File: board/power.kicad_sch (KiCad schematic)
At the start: 29 parts

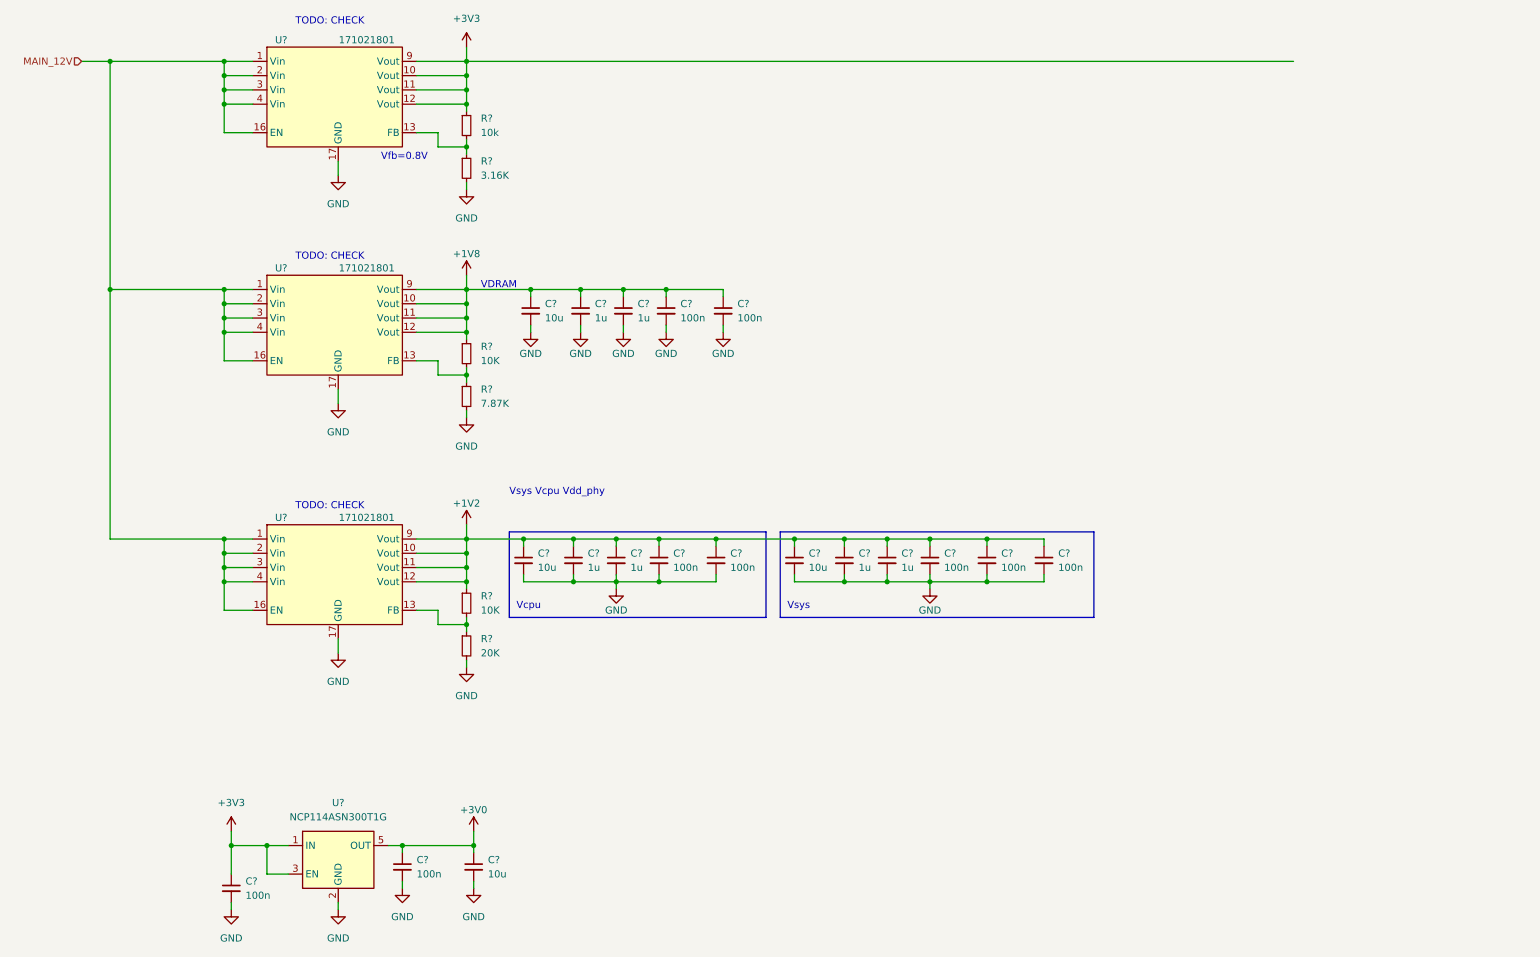
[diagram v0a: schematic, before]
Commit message: schematic update, choose components, creeate footprints
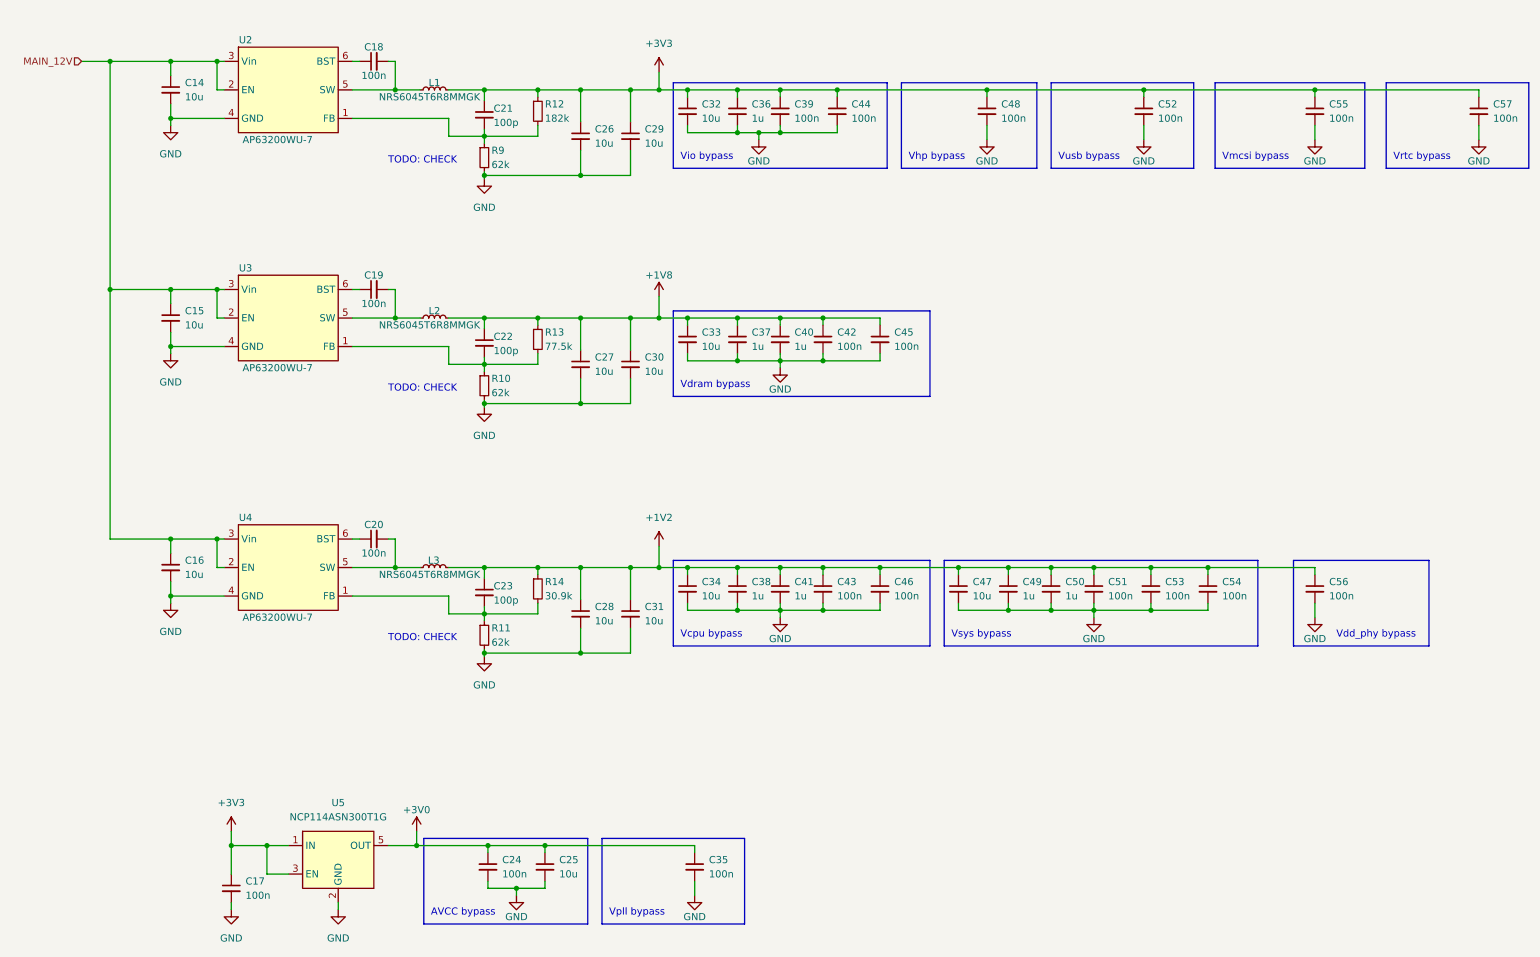
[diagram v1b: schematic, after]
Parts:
- removed R?: 3.16K, symbol Device:R_Small
- removed R? (x2): 10K, symbol Device:R_Small
- removed R?: 20K, symbol Device:R_Small
- removed R?: 7.87K, symbol Device:R_Small
- removed R?: 10k, symbol Device:R_Small
- removed U? (x3): 171021801, symbol v3s:171021801
- added C14, C15, C16, C26, C27, C28, C29, C30, C31, C32: 10u, Capacitor_SMD:C_0603_1608Metric, symbol Device:C_Small
- added C18, C19, C20, C35, C39, C44, C48, C52, C55, C56, C57: 100n, Capacitor_SMD:C_0603_1608Metric, symbol Device:C_Small
- added C21, C22, C23: 100p, Capacitor_SMD:C_0603_1608Metric, symbol Device:C_Small
- added C36: 1u, Capacitor_SMD:C_0603_1608Metric, symbol Device:C_Small
- added L1, L2, L3: NRS6045T6R8MMGK, v3s:NRS6045T6R8, symbol Device:L_Small
- added R10, R11, R9: 62k, Resistor_SMD:R_0603_1608Metric, symbol Device:R_Small
- added R12: 182k, Resistor_SMD:R_0603_1608Metric, symbol Device:R_Small
- added R13: 77.5k, Resistor_SMD:R_0603_1608Metric, symbol Device:R_Small
- added R14: 30.9k, Resistor_SMD:R_0603_1608Metric, symbol Device:R_Small
- added U2, U3, U4: AP63200WU-7, v3s:TSOT26, symbol v3s:AP63200WU-7
- C17, C24, C25, C33, C34, C37, C38, C40, C41, C42, C43, C45, C46, C47, C49, C50, C51, C53, C54: renamed from C?; footprint (none) -> Capacitor_SMD:C_0603_1608Metric
- gave numbers to parts that had none: 1
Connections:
- net +1V2: now also C23.1, C28.1, C31.1, C56.1, L3.2, R14.1
- net +1V8: now also C22.1, C27.1, C30.1, L2.2, R13.1
- net +3V0: now also C35.1
- net +3V3: now also C21.1, C26.1, C29.1, C32.1, C36.1, C39.1, C44.1, C48.1, C52.1, C55.1, C57.1, L1.2, R12.1
- net GND: now also C14.2, C15.2, C16.2, C26.2, C27.2, C28.2, C29.2, C30.2, C31.2, C32.2, C35.2, C36.2, C39.2, C44.2, C48.2, C52.2, C55.2, C56.2, C57.2, R10.2, R11.2, R9.2, U2.4 (GND), U3.4 (GND), U4.4 (GND)
- net MAIN_12V: now also C14.1, C15.1, C16.1, U2.2 (EN), U2.3 (Vin), U3.2 (EN), U3.3 (Vin), U4.2 (EN), U4.3 (Vin)
- new net: C19.1, U3.6 (BST)
- new net: C19.2, L2.1, U3.5 (SW)
- new net: C23.2, R11.1, R14.2, U4.1 (FB)
- new net: C20.2, L3.1, U4.5 (SW)
- new net: C20.1, U4.6 (BST)
- new net: C22.2, R10.1, R13.2, U3.1 (FB)
- new net: C18.2, L1.1, U2.5 (SW)
- new net: C21.2, R12.2, R9.1, U2.1 (FB)
- new net: C18.1, U2.6 (BST)
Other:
- note added: "AVCC bypass"
- note added: "Vcpu bypass"
- note added: "Vdd_phy bypass"
- note added: "Vdram bypass"
- note added: "Vhp bypass"
- note added: "Vio bypass"
- note added: "Vmcsi bypass"
- note added: "Vpll bypass"
- note added: "Vrtc bypass"
- note added: "Vsys bypass"
- note added: "Vusb bypass"
- note removed: "VDRAM"
- note removed: "Vcpu"
- note removed: "Vfb=0.8V"
- note removed: "Vsys"
- note removed: "Vsys Vcpu Vdd_phy"
- moved on the sheet: C24, C25, C33, C34, C37, C38, C40, C41, C42, C43, C45, C46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

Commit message: pcb layout
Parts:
- C25: value 10u -> 1u
- C32, C34, C47: value 10u -> 100n
- C36, C38, C41, C49, C50: value 1u -> 100n
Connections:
- net MAIN_12V renamed +12V
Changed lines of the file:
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@@
+    (stroke (width 0) (type default) (color 0 0 0 0))
+  )
+  (wire (pts (xy 30.48 27.94) (xy 30.48 30.48))
     (stroke (width 0) (type default) (color 0 0 0 0))
   )
@@
       (effects (font (size 1.27 1.27)) (justify left))
     )
-    (property "Value" "10u" (id 1) (at 135.89 40.6462 0)
+    (property "Value" "100n" (id 1) (at 135.89 40.6462 0)
       (effects (font (size 1.27 1.27)) (justify left))
     )
@@
       (effects (font (size 1.27 1.27)) (justify left))
     )
-    (property "Value" "10u" (id 1) (at 110.49 175.2662 0)
+    (property "Value" "1u" (id 1) (at 110.49 175.2662 0)
       (effects (font (size 1.27 1.27)) (justify left))
     )
@@
   )
   (symbol (lib_id "Device:C_Small") (at 205.74 124.46 0) (unit 1)
-    (in_bom yes) (on_board yes) (fields_autoplaced)
-    (property "Reference" "C51" (id 0) (at 208.28 123.1962 0)
-      (effects (font (size 1.27 1.27)) (justify left))
-    )
-    (property "Value" "100n" (id 1) (at 208.28 125.7362 0)
+    (in_bom yes) (on_board yes)
+    (property "Reference" "C51" (id 0) (at 207.645 123.19 0)
+      (effects (font (size 1.27 1.27)) (justify left))
+    )
+    (property "Value" "100n" (id 1) (at 207.645 125.73 0)
       (effects (font (size 1.27 1.27)) (justify left))
     )
@@
       (effects (font (size 1.27 1.27)) hide)
     )
-    (property "Datasheet" "https://ro.mouser.com/datasheet/2/396/wound04_e-1290968.pdf" (id 3) (at 88.265 120.65 0)
+    (property "Datasheet" "~" (id 3) (at 88.265 120.65 0)
       (effects (font (size 1.27 1.27)) hide)
     )
@@
       (effects (font (size 1.27 1.27)) (justify left))
     )
-    (property "Value" "10u" (id 1) (at 135.89 125.7362 0)
+    (property "Value" "100n" (id 1) (at 135.89 125.7362 0)
       (effects (font (size 1.27 1.27)) (justify left))
     )
@@
       (effects (font (size 1.27 1.27)) hide)
     )
-    (property "Datasheet" "https://ro.mouser.com/datasheet/2/396/wound04_e-1290968.pdf" (id 3) (at 88.265 76.2 0)
+    (property "Datasheet" "~" (id 3) (at 88.265 76.2 0)
       (effects (font (size 1.27 1.27)) hide)
     )
@@
       (effects (font (size 1.27 1.27)) (justify left))
     )
-    (property "Value" "1u" (id 1) (at 144.78 125.7362 0)
+    (property "Value" "100n" (id 1) (at 144.78 125.7362 0)
       (effects (font (size 1.27 1.27)) (justify left))
     )
@@
       (effects (font (size 1.27 1.27)) hide)
     )
-    (property "Datasheet" "https://ro.mouser.com/datasheet/2/396/wound04_e-1290968.pdf" (id 3) (at 88.265 35.56 0)
+    (property "Datasheet" "~" (id 3) (at 88.265 35.56 0)
       (effects (font (size 1.27 1.27)) hide)
     )
@@
   )
   (symbol (lib_id "Device:C_Small") (at 215.9 124.46 0) (unit 1)
-    (in_bom yes) (on_board yes) (fields_autoplaced)
+    (in_bom yes) (on_board yes)
     (property "Reference" "C53" (id 0) (at 218.44 123.1962 0)
       (effects (font (size 1.27 1.27)) (justify left))
@@
       (effects (font (size 1.27 1.27)) (justify left))
     )
-    (property "Value" "1u" (id 1) (at 193.04 125.7362 0)
+    (property "Value" "100n" (id 1) (at 193.04 125.7362 0)
       (effects (font (size 1.27 1.27)) (justify left))
     )
@@
       (effects (font (size 1.27 1.27)) (justify left))
     )
-    (property "Value" "1u" (id 1) (at 144.78 40.6462 0)
+    (property "Value" "100n" (id 1) (at 144.78 40.6462 0)
       (effects (font (size 1.27 1.27)) (justify left))
     )
@@
       (effects (font (size 1.27 1.27)) (justify left))
     )
-    (property "Value" "1u" (id 1) (at 152.4 125.7362 0)
+    (property "Value" "100n" (id 1) (at 152.4 125.7362 0)
       (effects (font (size 1.27 1.27)) (justify left))
     )
@@
       (effects (font (size 1.27 1.27)) (justify left))
     )
-    (property "Value" "10u" (id 1) (at 184.15 125.7362 0)
+    (property "Value" "100n" (id 1) (at 184.15 125.7362 0)
       (effects (font (size 1.27 1.27)) (justify left))
     )
@@
     (pin "2")
   )
+  (symbol (lib_id "power:+12V") (at 30.48 27.94 0) (unit 1)
+    (in_bom yes) (on_board yes)
+    (property "Reference" "#PWR0162" (id 0) (at 30.48 31.75 0)
+      (effects (font (size 1.27 1.27)) hide)
+    )
+    (property "Value" "+12V" (id 1) (at 30.48 24.13 0))
+    (property "Footprint" "" (id 2) (at 30.48 27.94 0)
+      (effects (font (size 1.27 1.27)) hide)
+    )
+    (property "Datasheet" "" (id 3) (at 30.48 27.94 0)
+      (effects (font (size 1.27 1.27)) hide)
+    )
+    (pin "1")
+  )
   (symbol (lib_id "Device:C_Small") (at 198.12 124.46 0) (unit 1)
-    (in_bom yes) (on_board yes) (fields_autoplaced)
-    (property "Reference" "C50" (id 0) (at 200.66 123.1962 0)
-      (effects (font (size 1.27 1.27)) (justify left))
-    )
-    (property "Value" "1u" (id 1) (at 200.66 125.7362 0)
-      (effects (font (size 1.27 1.27)) (justify left))
-    )
+    (in_bom yes) (on_board yes)
+    (property "Reference" "C50" (id 0) (at 200.025 123.19 0)
+      (effects (font (size 1.27 1.27)) (justify left))
+    )
+    (property "Value" "100n" (id 1) (at 200.025 125.73 0)
+      (effects (font (size 1.27 1.27)) (justify left))
+    )

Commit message: update layout
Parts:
- added R37, R38, R39: 1, Resistor_SMD:R_1206_3216Metric, symbol Device:R_Small
- C35: value 100n -> 1u
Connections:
- net +1V2: now also R39.2; no longer C23.1, C28.1, C31.1, L3.2, R14.1
- net +1V8: now also R38.2; no longer C22.1, C27.1, C30.1, L2.2, R13.1
- net +3V3: now also R37.2; no longer C21.1, C26.1, C29.1, L1.2, R12.1
- net SW_18: now reaches C19.2, L2.1, U3.5 (SW)
- net SW_12: now reaches C20.2, L3.1, U4.5 (SW)
- net SW_33: now reaches C18.2, L1.1, U2.5 (SW)
- new net: C21.1, C26.1, C29.1, L1.2, R12.1, R37.1
- new net: C23.1, C28.1, C31.1, L3.2, R14.1, R39.1
- new net: C22.1, C27.1, C30.1, L2.2, R13.1, R38.1
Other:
- moved on the sheet: C32, C33, C34, C36, C37, C38, C39, C40, C41, C42, C43, C44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

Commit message: updates, finish layout, remove usb-uart
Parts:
- L1, L2, L3: value NRS6045T6R8MMGK -> VLS6045AF-6R8M
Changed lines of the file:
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@@
     (in_bom yes) (on_board yes)
     (property "Reference" "L3" (id 0) (at 88.138 119.38 90))
-    (property "Value" "NRS6045T6R8MMGK" (id 1) (at 87.376 121.92 90))
+    (property "Value" "VLS6045AF-6R8M" (id 1) (at 87.376 121.92 90))
     (property "Footprint" "v3s:NRS6045T6R8" (id 2) (at 88.265 120.65 0)
       (effects (font (size 1.27 1.27)) hide)
@@
     (in_bom yes) (on_board yes)
     (property "Reference" "L2" (id 0) (at 88.265 74.93 90))
-    (property "Value" "NRS6045T6R8MMGK" (id 1) (at 87.376 77.47 90))
+    (property "Value" "VLS6045AF-6R8M" (id 1) (at 87.376 77.47 90))
     (property "Footprint" "v3s:NRS6045T6R8" (id 2) (at 88.265 76.2 0)
       (effects (font (size 1.27 1.27)) hide)
@@
     (in_bom yes) (on_board yes)
     (property "Reference" "L1" (id 0) (at 88.265 34.29 90))
-    (property "Value" "NRS6045T6R8MMGK" (id 1) (at 87.376 36.83 90))
+    (property "Value" "VLS6045AF-6R8M" (id 1) (at 87.376 36.83 90))
     (property "Footprint" "v3s:NRS6045T6R8" (id 2) (at 88.265 35.56 0)
       (effects (font (size 1.27 1.27)) hide)
